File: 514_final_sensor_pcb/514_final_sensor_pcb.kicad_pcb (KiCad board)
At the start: 2 copper layers, 48.8 x 28.2 mm, 6 parts, among them SW1 SW_SPDT, U1 ESP32C3

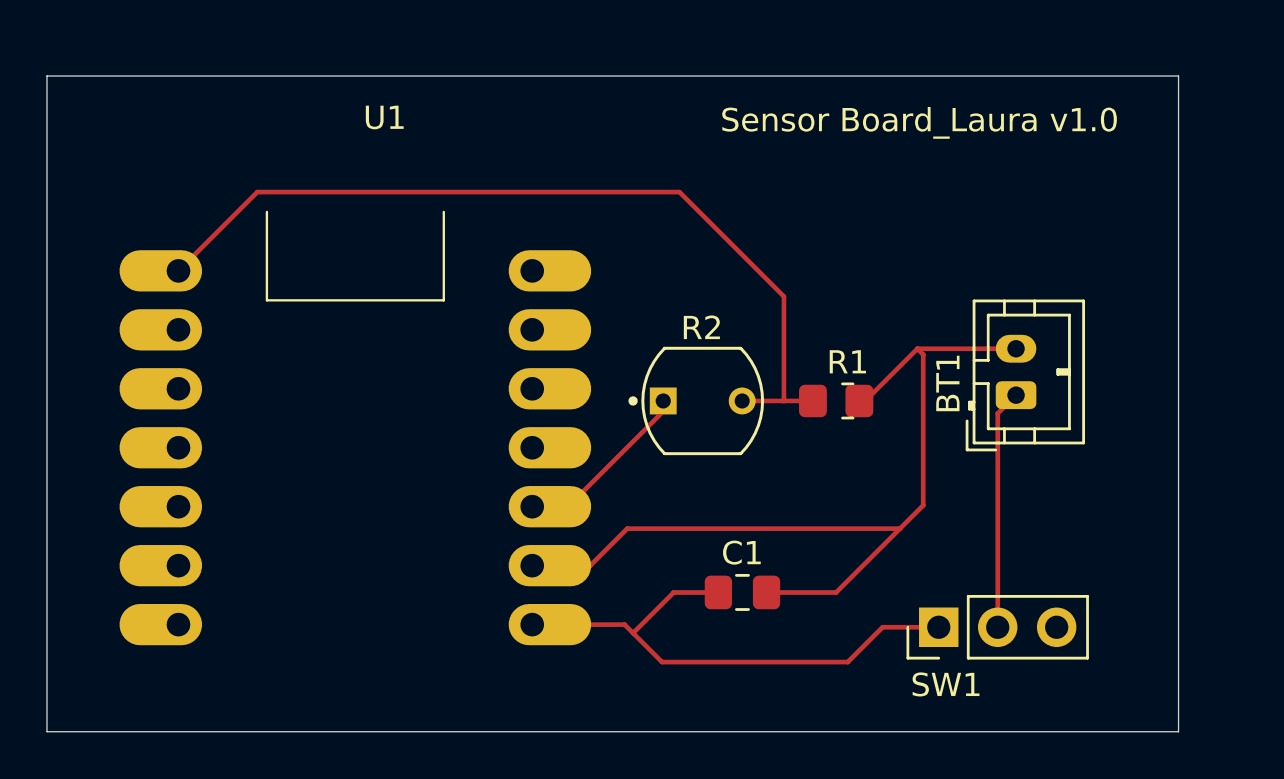
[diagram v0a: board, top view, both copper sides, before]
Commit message: battery estimate and datasheet update
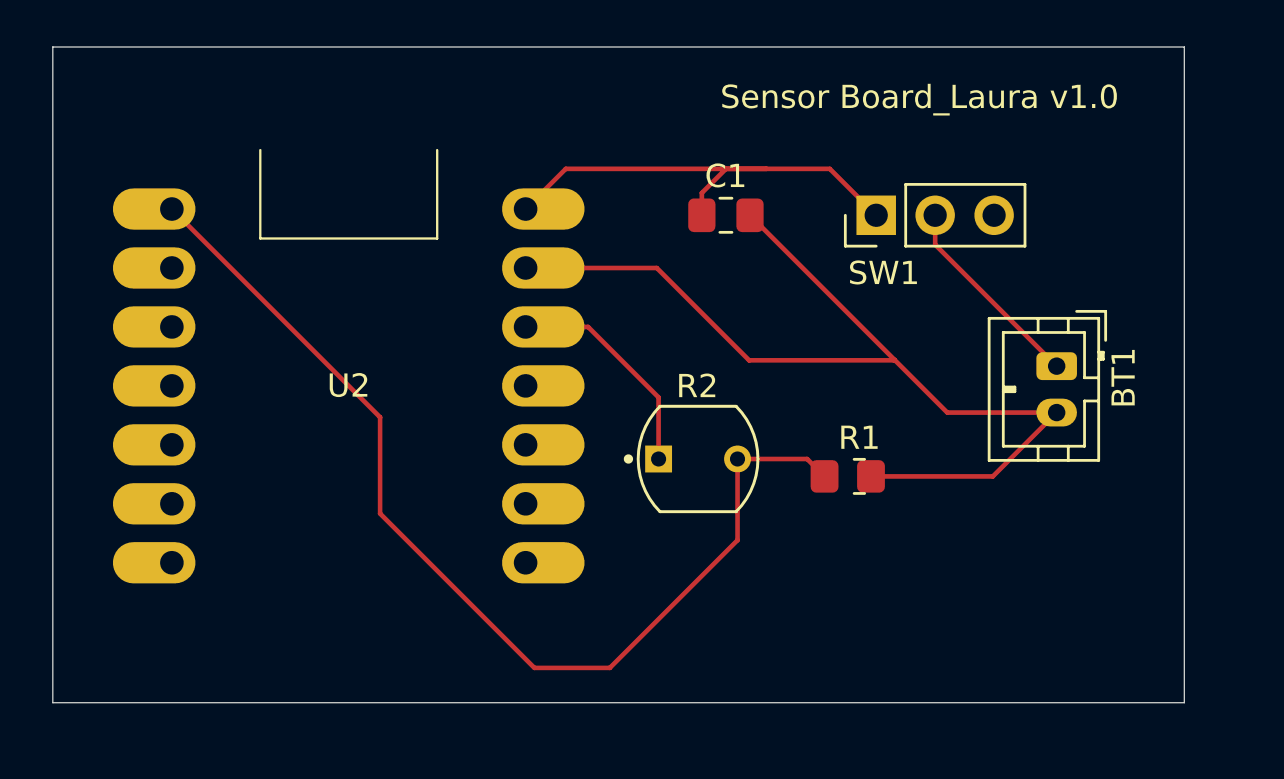
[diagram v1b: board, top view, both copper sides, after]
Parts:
- removed U1: ESP32C3, ESP32c3:XIAO_ESP32_SENSE
- added U2: ~, ESP32c3:XIAO_ESP32_SENSE, F.Cu at (82.0, 65.4)
- C1: value C -> 0.1uF
- R1: value R -> TBD
- R2: value CDS -> TBT
- moved SW1 18.0 mm to (104.7, 58.0)
- moved C1 16.3 mm to (98.2, 58.0)
- moved R1 3.29 mm to (104.0, 69.2)
- moved R2 2.51 mm to (97.0, 68.5)
- moved BT1 2.15 mm to (112.5, 64.5), turned to -90 degrees
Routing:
- net Net-(U2-GPIO1_A0_D0): track 37.9 -> 44.8 mm
- net Net-(BT1--): track 39.4 -> 43.4 mm
- net Net-(SW1-A): track 23.4 -> 20.8 mm
- net Net-(BT1-+): track 10.3 -> 8.67 mm

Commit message: second device
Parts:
- moved BT1 0.79 mm to (113.2, 64.8)
- moved C1 0.79 mm to (99.0, 58.2)
- moved R1 0.79 mm to (104.8, 69.5)
- moved R2 0.79 mm to (97.8, 68.8)
- moved SW1 0.79 mm to (105.5, 58.2)
- moved U2 0.79 mm to (82.8, 65.6)
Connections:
- net Net-(BT1--) renamed GND
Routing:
- net GND: track 43.4 -> 0.00 mm
- added copper zone on B.Cu, net GND
- added copper zone on F.Cu, net GND
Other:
- board size 48.8 x 28.2 mm -> 48.8 x 27.2 mm
- board text added: "Sensor Board_Laura v1.1"
- board text removed: "Sensor Board_Laura v1.0"
